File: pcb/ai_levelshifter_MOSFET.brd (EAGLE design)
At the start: 15.2 x 14 mm, 15 parts, among them J1 1X06, J2 1X06NOFIRST, Q1 BSS138, Q2 BSS138, Q3 BSS138, Q4 BSS138

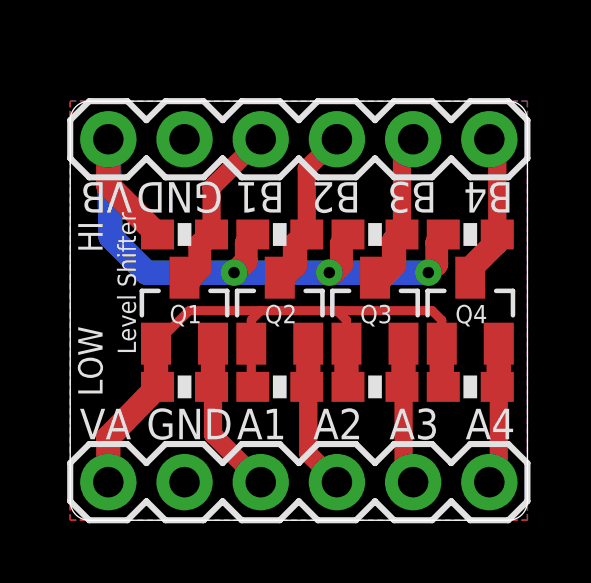
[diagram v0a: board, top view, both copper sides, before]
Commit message: fixed spacing to fit properly on a breadboard
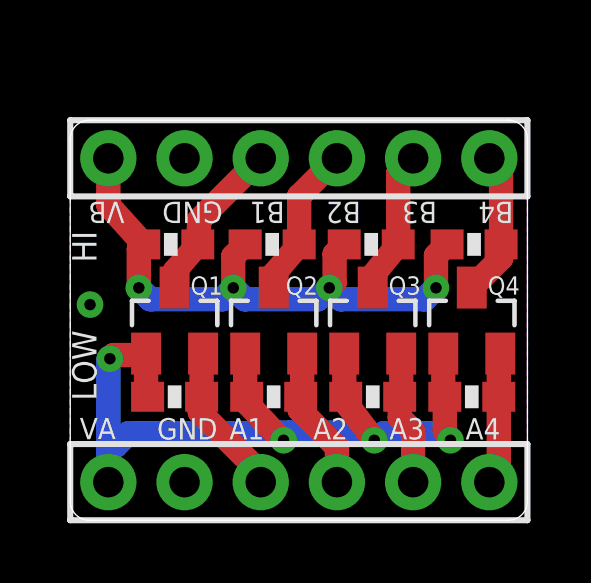
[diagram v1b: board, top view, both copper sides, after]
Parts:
- moved J2 0.63 mm to (7.62, 12.1)
- moved R2 0.56 mm to (3.35, 9.19)
- moved Q1 0.47 mm to (3.48, 6.65)
- moved R1 0.47 mm to (3.48, 4.11)
- moved R4 0.42 mm to (6.73, 9.19)
- moved Q2 0.39 mm to (6.78, 6.65)
- moved R3 0.39 mm to (6.78, 4.11)
- moved R6 0.35 mm to (10.0, 9.19)
- moved R8 0.35 mm to (13.5, 9.19)
- moved Q3 0.34 mm to (10.1, 6.65)
- moved R5 0.34 mm to (10.1, 4.11)
- moved Q4 0.33 mm to (13.4, 6.65)
- moved R7 0.33 mm to (13.4, 4.11)
- moved U$1 0.22 mm to (8.97, 8.38)
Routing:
- net VCC-A: track 24.6 -> 28.9 mm, vias 0 -> 4
- net VCC-B: track 22.8 -> 20.6 mm, vias 3 -> 4
- added copper zone on layer 1, net GND
- removed copper zone on layer 1, net N$1
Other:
- board size 15.2 x 14 mm -> 15.2 x 13.3 mm
- board text removed: "Level Shifter"

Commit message: updating
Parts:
- moved J2 1.91 mm to (7.62, 14.0)
- moved Q1 1.27 mm to (3.48, 7.92)
- moved Q2 1.27 mm to (6.78, 7.92)
- moved Q3 1.27 mm to (10.1, 7.92)
- moved Q4 1.27 mm to (13.4, 7.92)
- moved R2 1.27 mm to (3.35, 10.5)
- moved R4 1.27 mm to (6.73, 10.5)
- moved R6 1.27 mm to (10.0, 10.5)
- moved R8 1.27 mm to (13.5, 10.5)
- moved U$1 1.27 mm to (8.97, 9.65)
- moved R1 0.63 mm to (3.48, 4.75)
- moved R3 0.63 mm to (6.78, 4.75)
- moved R5 0.63 mm to (10.1, 4.75)
- moved R7 0.63 mm to (13.4, 4.75)
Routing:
- net VCC-A: track 28.9 -> 35.3 mm
- net A3: track 4.49 -> 5.76 mm
- net A2: track 4.84 -> 6.11 mm
- net A1: track 5.17 -> 6.42 mm
- net A4: track 4.44 -> 5.69 mm
- net VCC-B: track 20.6 -> 21.3 mm
- net B1: track 5.45 -> 6.10 mm
- net B3: track 4.84 -> 5.48 mm
- net B2: track 5.13 -> 5.77 mm
- net B4: track 4.88 -> 5.51 mm
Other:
- board size 15.2 x 13.3 mm -> 15.2 x 15.2 mm
- board text added: "v1.1"
- board text removed: "v1.0"
